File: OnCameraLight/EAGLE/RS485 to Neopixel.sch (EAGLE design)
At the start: 10 parts, among them IC1 75176AP

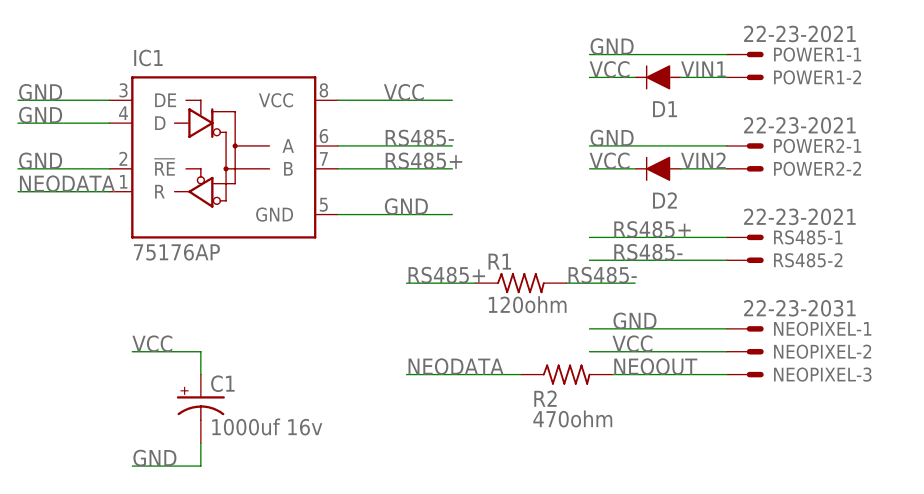
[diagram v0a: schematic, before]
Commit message: Go through and fix notation on RS485 wiring everywhere to use the standard A/B notation.
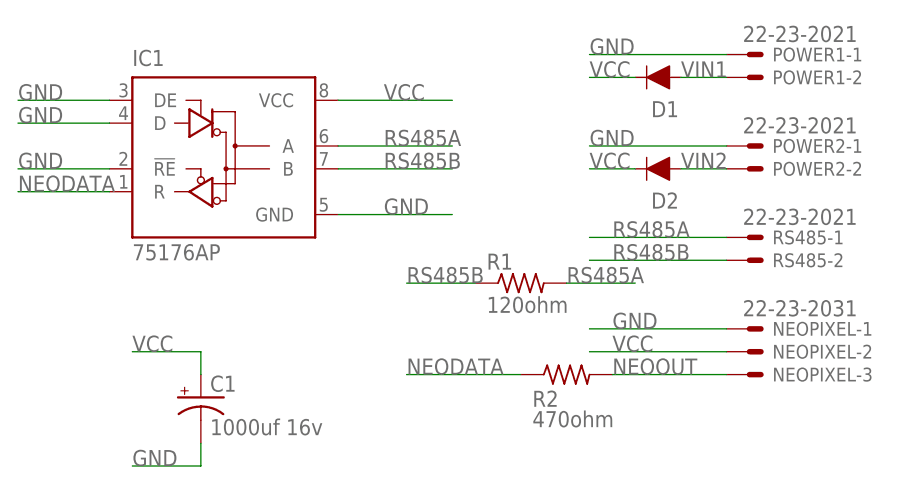
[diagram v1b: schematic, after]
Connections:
- removed net RS485+: IC1.B, R1.1, RS485-1.S
- removed net RS485-: IC1.A, R1.2, RS485-2.S
- new net RS485A: IC1.A, R1.2, RS485-1.S
- new net RS485B: IC1.B, R1.1, RS485-2.S
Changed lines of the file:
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@@
-</segment>
-</net>
-<net name="RS485+" class="0">
-<segment>
-<pinref part="RS485" gate="-1" pin="S"/>
-<wire x1="134.62" y1="127" x2="119.38" y2="127" width="0.1524" layer="91"/>
-<label x="121.92" y="127" size="1.778" layer="95"/>
-</segment>
-<segment>
-<pinref part="R1" gate="G$1" pin="1"/>
-<wire x1="106.68" y1="121.92" x2="99.06" y2="121.92" width="0.1524" layer="91"/>
-<label x="99.06" y="121.92" size="1.778" layer="95"/>
-</segment>
-<segment>
-<pinref part="IC1" gate="G$1" pin="B"/>
-<wire x1="91.44" y1="134.62" x2="104.14" y2="134.62" width="0.1524" layer="91"/>
-<label x="96.52" y="134.62" size="1.778" layer="95"/>
-</segment>
-</net>
-<net name="RS485-" class="0">
-<segment>
-<pinref part="RS485" gate="-2" pin="S"/>
-<wire x1="134.62" y1="124.46" x2="119.38" y2="124.46" width="0.1524" layer="91"/>
-<label x="121.92" y="124.46" size="1.778" layer="95"/>
-</segment>
-<segment>
-<pinref part="R1" gate="G$1" pin="2"/>
-<wire x1="116.84" y1="121.92" x2="124.46" y2="121.92" width="0.1524" layer="91"/>
-<label x="116.84" y="121.92" size="1.778" layer="95"/>
-</segment>
-<segment>
-<pinref part="IC1" gate="G$1" pin="A"/>
-<wire x1="91.44" y1="137.16" x2="104.14" y2="137.16" width="0.1524" layer="91"/>
-<label x="96.52" y="137.16" size="1.778" layer="95"/>
 </segment>
 </net>
@@
 </segment>
 </net>
+<net name="RS485B" class="0">
+<segment>
+<pinref part="IC1" gate="G$1" pin="B"/>
+<wire x1="91.44" y1="134.62" x2="104.14" y2="134.62" width="0.1524" layer="91"/>
+<label x="96.52" y="134.62" size="1.778" layer="95"/>
+</segment>
+<segment>
+<pinref part="R1" gate="G$1" pin="1"/>
+<wire x1="106.68" y1="121.92" x2="99.06" y2="121.92" width="0.1524" layer="91"/>
+<label x="99.06" y="121.92" size="1.778" layer="95"/>
+</segment>
+<segment>
+<pinref part="RS485" gate="-2" pin="S"/>
+<wire x1="134.62" y1="124.46" x2="119.38" y2="124.46" width="0.1524" layer="91"/>
+<label x="121.92" y="124.46" size="1.778" layer="95"/>
+</segment>
+</net>
+<net name="RS485A" class="0">
+<segment>
+<pinref part="IC1" gate="G$1" pin="A"/>
+<wire x1="91.44" y1="137.16" x2="104.14" y2="137.16" width="0.1524" layer="91"/>
+<label x="96.52" y="137.16" size="1.778" layer="95"/>
+</segment>
+<segment>
+<pinref part="R1" gate="G$1" pin="2"/>
+<wire x1="116.84" y1="121.92" x2="124.46" y2="121.92" width="0.1524" layer="91"/>
+<label x="116.84" y="121.92" size="1.778" layer="95"/>
+</segment>
+<segment>
+<pinref part="RS485" gate="-1" pin="S"/>
+<wire x1="134.62" y1="127" x2="119.38" y2="127" width="0.1524" layer="91"/>
+<label x="121.92" y="127" size="1.778" layer="95"/>
+</segment>
+</net>
